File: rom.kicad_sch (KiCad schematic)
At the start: 3 parts, among them IC17 27C256, IC18 74LS08

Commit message: handle 27C512
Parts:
- added JP6: ROM A14, Dragon:Jumper_4, symbol vdg:Jumper_4
- added JP7: 27C512, Jumper:SolderJumper-3_P1.3mm_Open_Pad1.0x1.5mm, symbol Jumper:SolderJumper_3_Open
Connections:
- net +5V: now also JP6.1 (A)
- net GND: now also JP6.2 (B), JP7.1 (A); no longer IC17.1 (VPP)
- net ~{ROM}: now also JP7.3 (B); no longer IC17.22 (~{OE})
- net at IC17.27 (A14): now also JP6.4 (Out); no longer JP1.2 (C)
- new net MEM-SIZE: JP6.3 (C)
- new net ROM-A15: IC17.1 (VPP), JP1.2 (C)
- new net VPP: IC17.22 (~{OE}), JP7.2 (C)
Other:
- moved on the sheet: JP1

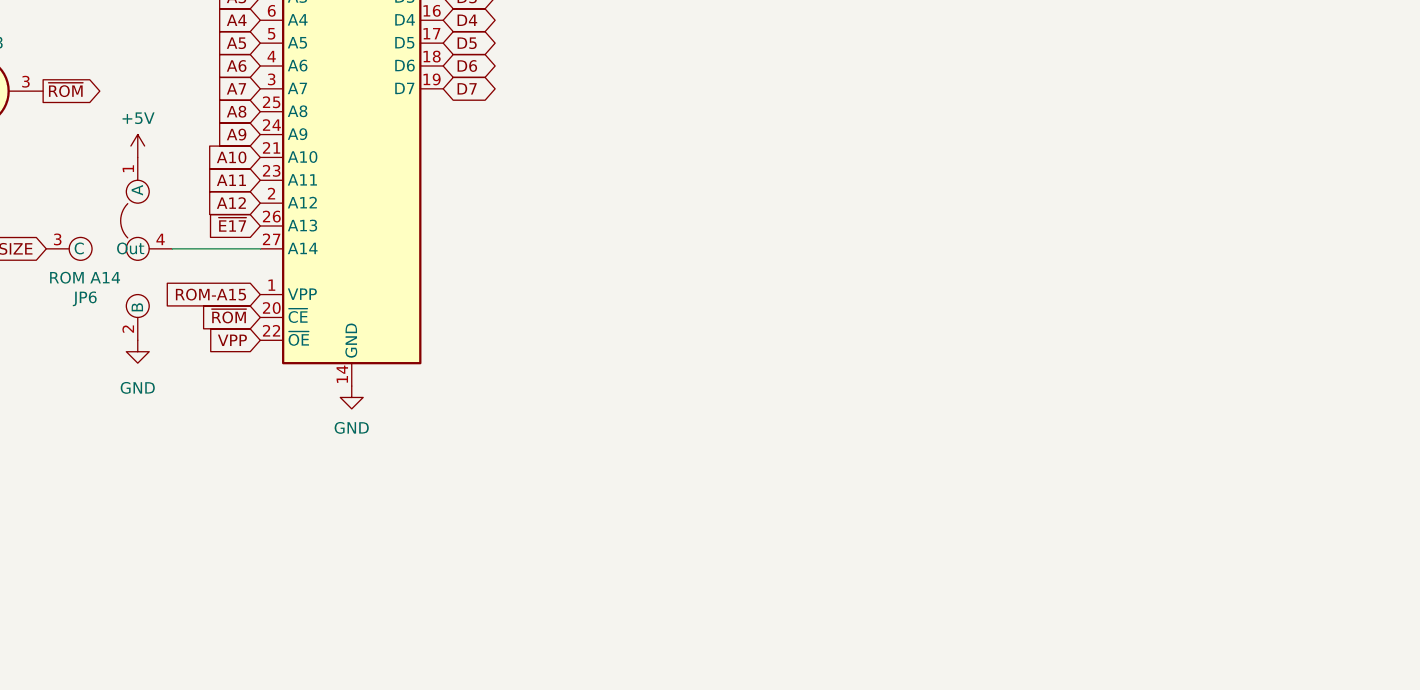
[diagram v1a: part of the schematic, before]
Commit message: fix rom and pia select traces
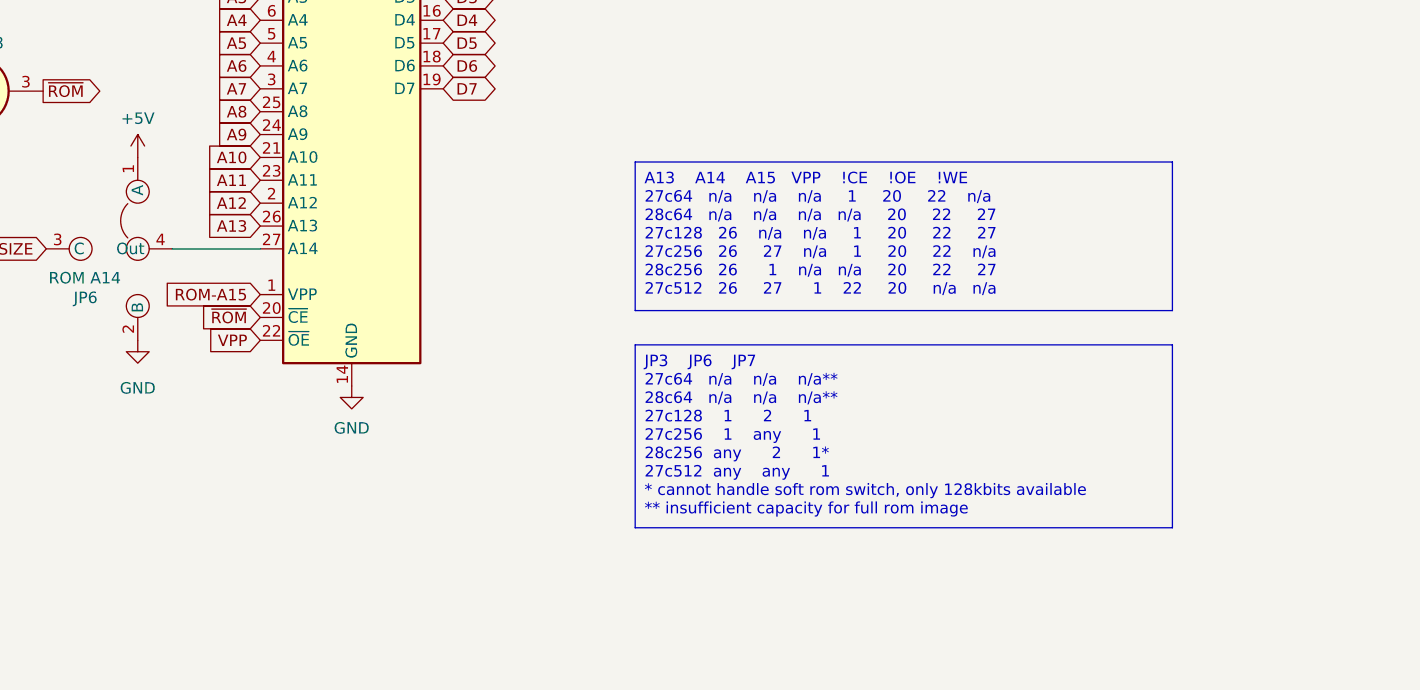
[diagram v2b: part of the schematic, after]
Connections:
- net ~{E17}: no longer IC17.26 (A13)
- new net A13: IC17.26 (A13)
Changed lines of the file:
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@@
     (stroke (width 0) (type default))
+  )
+  (text_box "        JP3    JP6    JP7\n27c64   n/a    n/a    n/a**\n28c64   n/a    n/a    n/a**\n27c128    1      2      1\n27c256    1    any      1\n28c256  any      2      1*\n27c512  any    any      1\n* cannot handle soft rom switch, only 128kbits available\n** insufficient capacity for full rom image\n    "
+    (at 165.1 189.23 0) (size 59.69 20.32)
+    (stroke (width 0) (type default))
+    (fill (type none))
+    (effects (font (face "Consolas") (size 1.27 1.27)) (justify left top))
+  )
+  (text_box "        A13    A14    A15   VPP    !CE    !OE    !WE\n27c64   n/a    n/a    n/a     1     20     22    n/a\n28c64   n/a    n/a    n/a   n/a     20     22     27\n27c128   26    n/a    n/a     1     20     22     27\n27c256   26     27    n/a     1     20     22    n/a\n28c256   26      1    n/a   n/a     20     22     27\n27c512   26     27      1    22     20     n/a   n/a\n    "
+    (at 165.1 168.91 0) (size 59.69 16.51)
+    (stroke (width 0) (type default))
+    (fill (type none))
+    (effects (font (face "Consolas") (size 1.27 1.27)) (justify left top))
   )
   (global_label "D7" (shape bidirectional) (at 143.764 160.782 0) (fields_autoplaced)
@@
     )
   )
-  (global_label "~{E17}" (shape input) (at 123.444 176.022 180) (fields_autoplaced)
+  (global_label "A13" (shape input) (at 123.444 176.022 180) (fields_autoplaced)
     (effects (font (size 1.27 1.27)) (justify right))
-    (property "Intersheetrefs" "${INTERSHEET_REFS}" (at 117.5517 175.9426 0)
+    (property "Intersheetrefs" "${INTERSHEET_REFS}" (at 117.6054 176.022 0)
       (effects (font (size 1.27 1.27)) (justify right) hide)
     )

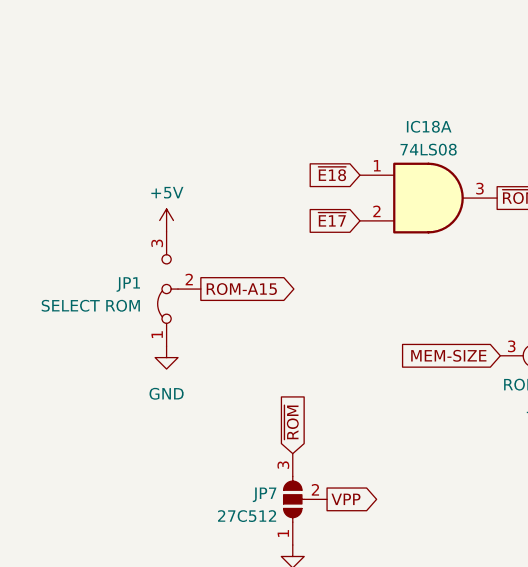
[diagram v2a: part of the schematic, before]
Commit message: reinforce audio traces
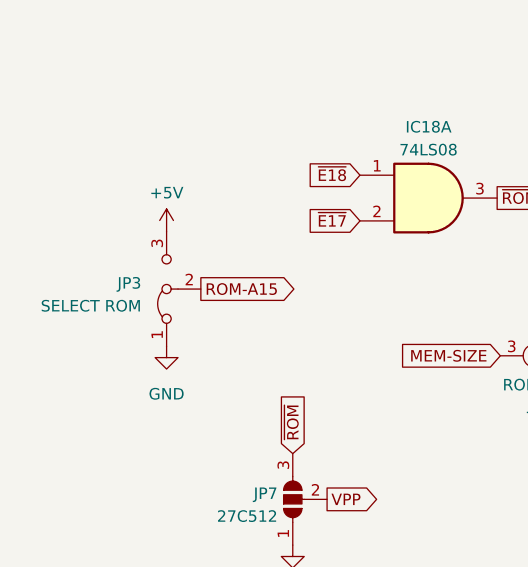
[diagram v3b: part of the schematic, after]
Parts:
- renumbered JP1 to JP3
